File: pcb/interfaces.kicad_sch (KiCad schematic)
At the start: 12 parts

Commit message: Updates for consistency
Changed mounting holes to grounded
Updated power connectors
Added power ESD protection
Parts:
- removed D1: PESD5V5C1BL, CRGM Passive:DFN1006-2, symbol CRGM Passive:PESD5V5C1BLYL
- removed D2: PESD3V3S1BL, CRGM Passive:DFN1006-2, symbol CRGM Passive:PESD3V3S1BL
- removed J5, J6: ~, CRGM Connector:JST_SH_SM04B-SRSS-TB_1x04-1MP_P1.00mm_Horizontal, symbol CRGM Connector:AQ_POWER
- removed TP15, TP16, TP17: ~, CRGM Mechanical:TestPoint_Pad_D1.0mm, symbol Connector:TestPoint
- J4: now not fitted; now left out of the parts list
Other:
- note removed: "Power"

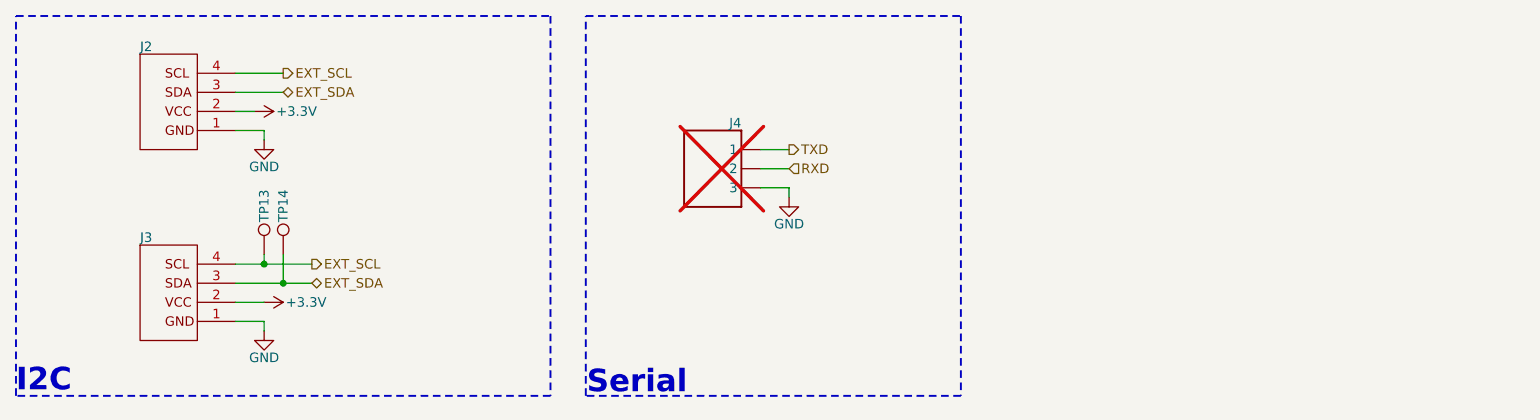
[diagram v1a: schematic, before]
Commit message: Switched back to global lables
Updated all gnd and test point symbols
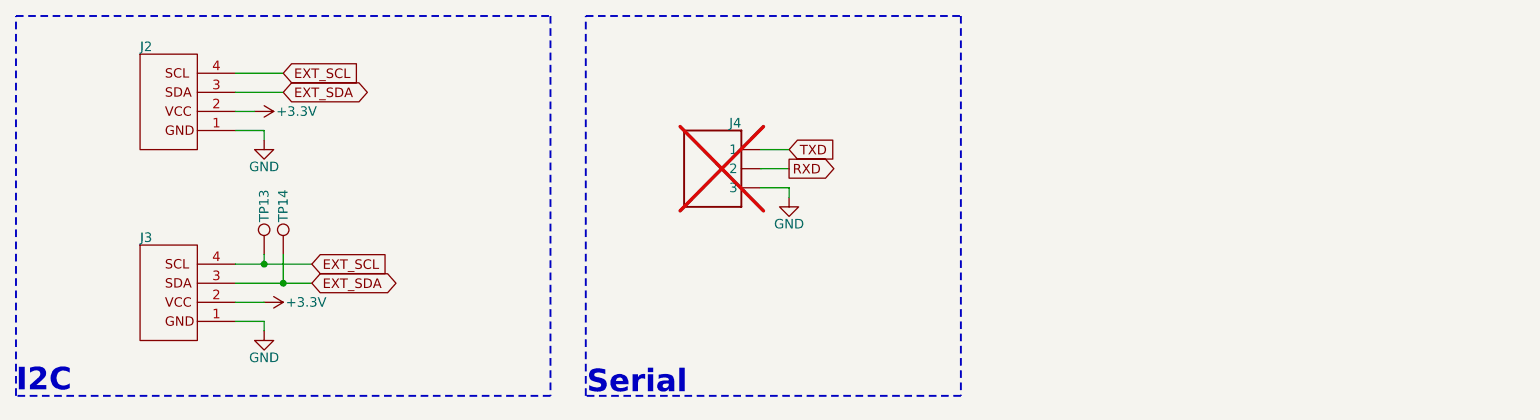
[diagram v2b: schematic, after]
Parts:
- TP13, TP14: symbol Connector:TestPoint -> CRGM Connector:TestPoint
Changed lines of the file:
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@@
 		)
 	)
-	(hierarchical_label "EXT_SDA"
-		(shape bidirectional)
-		(at 64.77 60.96 0)
+	(global_label "RXD"
+		(shape output)
+		(at 128.27 45.72 0)
+		(fields_autoplaced yes)
 		(effects
 			(font
@@
 			(justify left)
 		)
-	)
-	(hierarchical_label "EXT_SCL"
-		(shape output)
-		(at 64.77 58.42 0)
+		(property "Intersheetrefs" "${INTERSHEET_REFS}"
+			(at 135.0047 45.72 0)
+			(effects
+				(font
+					(size 1.27 1.27)
+				)
+				(justify left)
+			)
+		)
+	)
+	(global_label "TXD"
+		(shape input)
+		(at 128.27 43.18 0)
+		(fields_autoplaced yes)
 		(effects
 			(font
@@
 			(justify left)
 		)
-	)
-	(hierarchical_label "EXT_SDA"
+		(property "Intersheetrefs" "${INTERSHEET_REFS}"
+			(at 134.7023 43.18 0)
+			(effects
+				(font
+					(size 1.27 1.27)
+				)
+				(justify left)
+			)
+		)
+	)
+	(global_label "EXT_SDA"
 		(shape bidirectional)
-		(at 60.96 35.56 0)
+		(at 64.77 60.96 0)
+		(fields_autoplaced yes)
 		(effects
 			(font
@@
 			(justify left)
 		)
-	)
-	(hierarchical_label "RXD"
+		(property "Intersheetrefs" "${INTERSHEET_REFS}"
+			(at 76.7283 60.96 0)
+			(effects
+				(font
+					(size 1.27 1.27)
+				)
+				(justify left)
+			)
+		)
+	)
+	(global_label "EXT_SCL"
 		(shape input)
-		(at 128.27 45.72 0)
+		(at 64.77 58.42 0)
+		(fields_autoplaced yes)
 		(effects
 			(font
@@
 			(justify left)
 		)
-	)
-	(hierarchical_label "EXT_SCL"
-		(shape output)
-		(at 60.96 33.02 0)
+		(property "Intersheetrefs" "${INTERSHEET_REFS}"
+			(at 75.5565 58.42 0)
+			(effects
+				(font
+					(size 1.27 1.27)
+				)
+				(justify left)
+			)
+		)
+	)
+	(global_label "EXT_SDA"
+		(shape bidirectional)
+		(at 60.96 35.56 0)
+		(fields_autoplaced yes)
 		(effects
 			(font
@@
 			(justify left)
 		)
-	)
-	(hierarchical_label "TXD"
-		(shape output)
-		(at 128.27 43.18 0)
+		(property "Intersheetrefs" "${INTERSHEET_REFS}"
+			(at 72.9183 35.56 0)
+			(effects
+				(font
+					(size 1.27 1.27)
+				)
+				(justify left)
+			)
+		)
+	)
+	(global_label "EXT_SCL"
+		(shape input)
+		(at 60.96 33.02 0)
+		(fields_autoplaced yes)
 		(effects
 			(font
@@
 			)
 			(justify left)
+		)
+		(property "Intersheetrefs" "${INTERSHEET_REFS}"
+			(at 71.7465 33.02 0)
+			(effects
+				(font
+					(size 1.27 1.27)
+				)
+				(justify left)
+			)
 		)
 	)
@@
 	)
 	(symbol
-		(lib_id "Connector:TestPoint")
+		(lib_id "CRGM Connector:TestPoint")
 		(at 60.96 57.15 0)
 		(unit 1)
@@
 		)
 		(property "Footprint" "CRGM Mechanical:TestPoint_Pad_D1.0mm"
-			(at 66.04 57.15 0)
+			(at 60.96 64.516 0)
 			(effects
 				(font
@@
 		)
 		(property "Datasheet" "~"
-			(at 66.04 57.15 0)
-			(effects
-				(font
-					(size 1.27 1.27)
-				)
-				(hide yes)
-			)
-		)
-		(property "Description" "test point"
-			(at 60.96 57.15 0)
+			(at 63.246 55.118 0)
+			(effects
+				(font
+					(size 1.27 1.27)
+				)
+				(hide yes)
+			)
+		)
+		(property "Description" "Test Point D1.0mm"
+			(at 60.96 66.294 0)
 			(effects
 				(font
@@
 	)
 	(symbol
-		(lib_id "Connector:TestPoint")
+		(lib_id "CRGM Connector:TestPoint")
 		(at 58.42 57.15 0)
 		(unit 1)
@@
 		)
 		(property "Footprint" "CRGM Mechanical:TestPoint_Pad_D1.0mm"
-			(at 63.5 57.15 0)
+			(at 58.42 64.516 0)
 			(effects
 				(font
@@
 		)
 		(property "Datasheet" "~"
-			(at 63.5 57.15 0)
-			(effects
-				(font
-					(size 1.27 1.27)
-				)
-				(hide yes)
-			)
-		)
-		(property "Description" "test point"
-			(at 58.42 57.15 0)
-			(effects
-				(font
+			(at 60.706 55.118 0)
+			(effects
+				(font
+					(size 1.27 1.27)
+				)
+				(hide yes)
+			)
+		)
+		(property "Description" "Test Point D1.0mm"
+			(at 58.42 66.294 0)
+			(effects
+				(font
